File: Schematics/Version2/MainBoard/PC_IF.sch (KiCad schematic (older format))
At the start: 4 parts, among them U22 74F574, U23 74F574

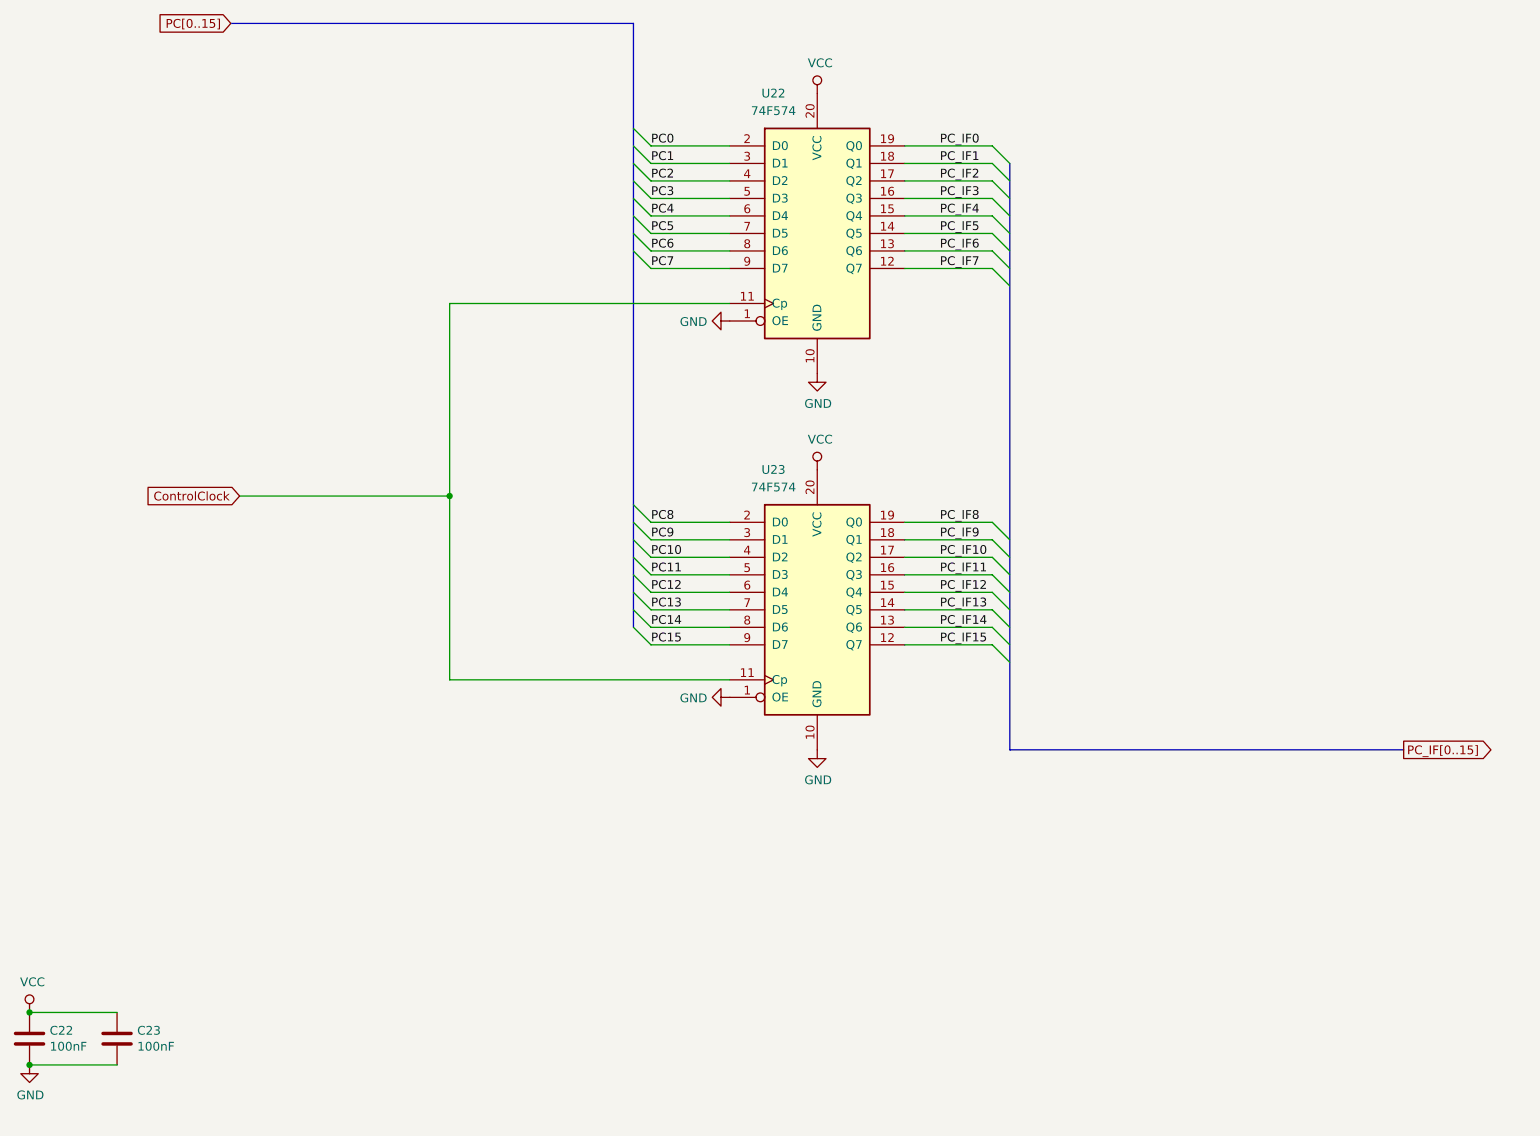
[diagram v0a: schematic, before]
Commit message: Merge branch "version2a"
This replaces the Version2 schematics with a new second version. This one
completes a four layer routing of the main board.
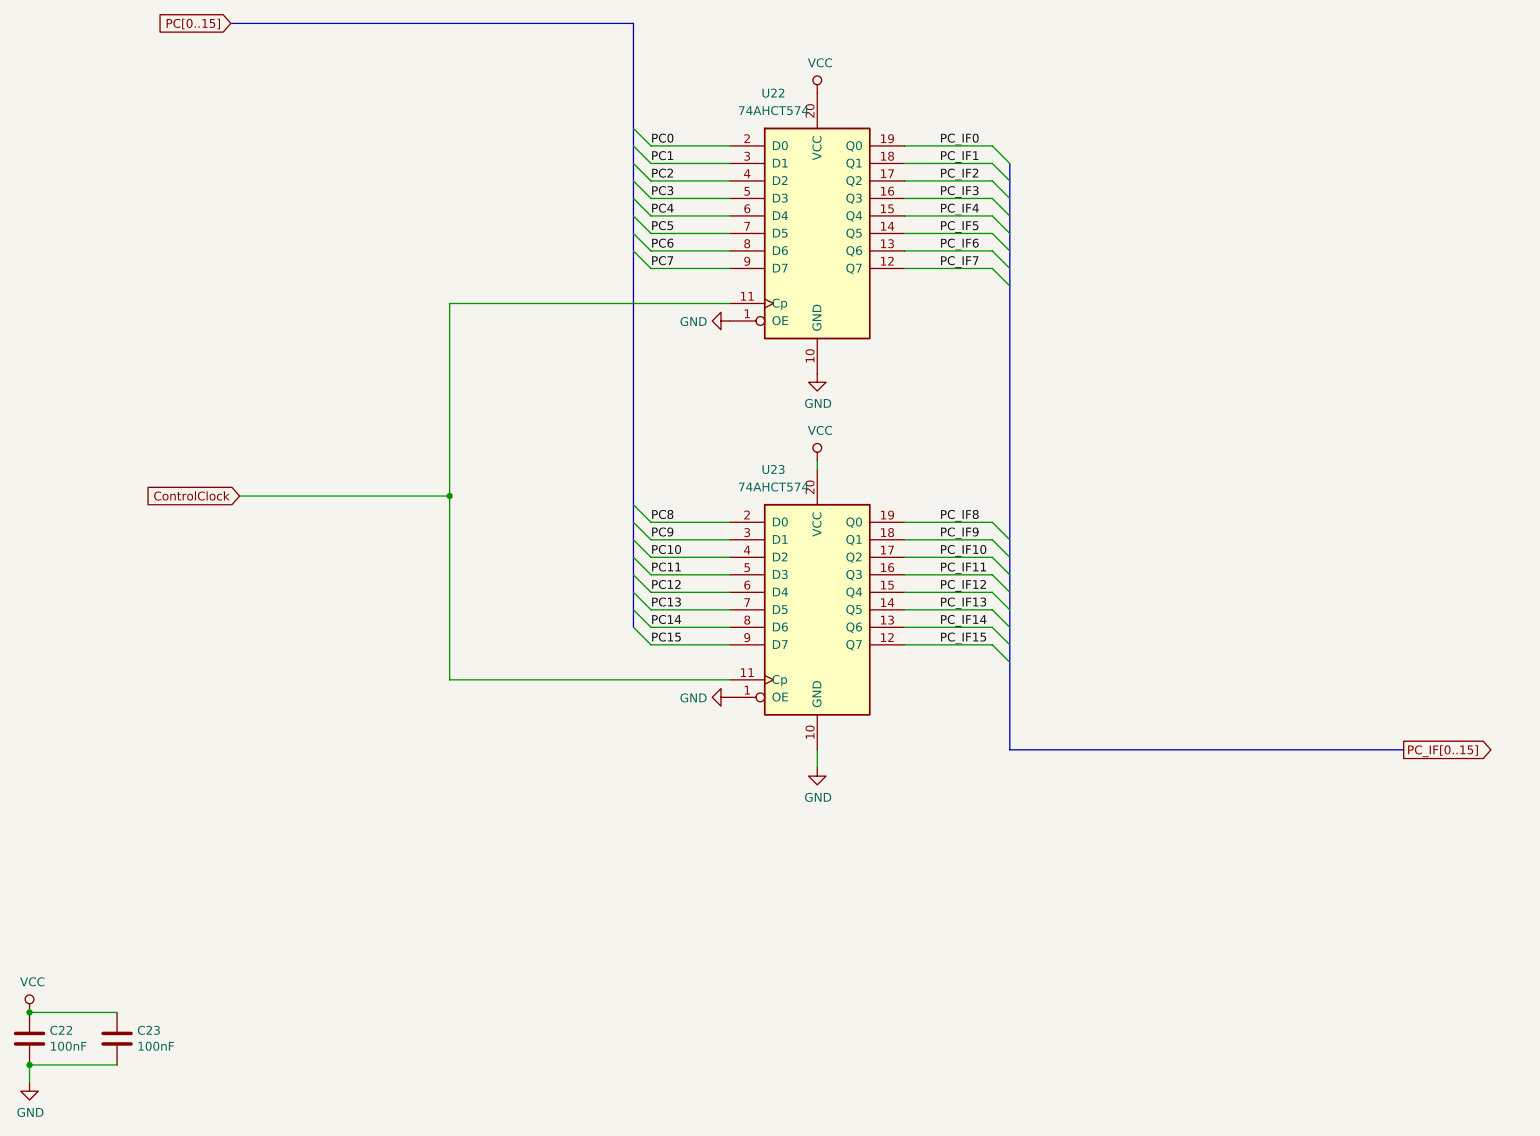
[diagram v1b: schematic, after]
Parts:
- U22, U23: value 74F574 -> 74AHCT574
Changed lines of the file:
@@
 $Descr USLetter 11000 8500
 encoding utf-8
-Sheet 6 22
+Sheet 6 23
 Title "PC/IF"
 Date ""
@@
 $EndComp
 $Comp
-L power:VCC #PWR058
-U 1 1 5DD11404
-P 5500 3900
-F 0 "#PWR058" H 5500 3750 50  0001 C CNN
-F 1 "VCC" H 5517 4073 50  0000 C CNN
-F 2 "" H 5500 3900 50  0001 C CNN
-F 3 "" H 5500 3900 50  0001 C CNN
-	1    5500 3900
-	1    0    0    -1
-$EndComp
-$Comp
 L power:GND #PWR057
 U 1 1 5DD11B50
@@
 L power:GND #PWR059
 U 1 1 5DD12126
-P 5500 5500
-F 0 "#PWR059" H 5500 5250 50  0001 C CNN
-F 1 "GND" H 5505 5327 50  0000 C CNN
-F 2 "" H 5500 5500 50  0001 C CNN
-F 3 "" H 5500 5500 50  0001 C CNN
-	1    5500 5500
+P 5500 5600
+F 0 "#PWR059" H 5500 5350 50  0001 C CNN
+F 1 "GND" H 5505 5427 50  0000 C CNN
+F 2 "" H 5500 5600 50  0001 C CNN
+F 3 "" H 5500 5600 50  0001 C CNN
+	1    5500 5600
 	1    0    0    -1
 $EndComp
@@
 $EndComp
 $Comp
-L power:GND #PWR053
-U 1 1 5DD314A1
-P 1000 7300
-F 0 "#PWR053" H 1000 7050 50  0001 C CNN
-F 1 "GND" H 1005 7127 50  0000 C CNN
-F 2 "" H 1000 7300 50  0001 C CNN
-F 3 "" H 1000 7300 50  0001 C CNN
-	1    1000 7300
-	1    0    0    -1
-$EndComp
-$Comp
 L power:VCC #PWR052
 U 1 1 5DD314A7
@@
 Wire Wire Line
 	1500 7300 1000 7300
-Connection ~ 1000 7300
 $Comp
 L 74xx:74LS574 U?
@@
 AR Path="/5D8005AF/5D833E4B/5D89A6E8" Ref="U22"  Part="1"
 F 0 "U22" H 5250 3350 50  0000 C CNN
-F 1 "74F574" H 5250 3250 50  0000 C CNN
+F 1 "74AHCT574" H 5250 3250 50  0000 C CNN
 F 2 "Package_DIP:DIP-20_W7.62mm" H 5500 2550 50  0001 C CNN
-F 3 "http://www.ti.com/lit/gpn/sn74LS574" H 5500 2550 50  0001 C CNN
+F 3 "http://www.ti.com/lit/ds/symlink/sn74ahct574.pdf" H 5500 2550 50  0001 C CNN
 	1    5500 2550
 	1    0    0    -1
@@
 AR Path="/5D8005AF/5D833E4B/5D89C1BF" Ref="U23"  Part="1"
 F 0 "U23" H 5250 5500 50  0000 C CNN
-F 1 "74F574" H 5250 5400 50  0000 C CNN
+F 1 "74AHCT574" H 5250 5400 50  0000 C CNN
 F 2 "Package_DIP:DIP-20_W7.62mm" H 5500 4700 50  0001 C CNN
-F 3 "http://www.ti.com/lit/gpn/sn74LS574" H 5500 4700 50  0001 C CNN
+F 3 "http://www.ti.com/lit/ds/symlink/sn74ahct574.pdf" H 5500 4700 50  0001 C CNN
 	1    5500 4700
 	1    0    0    -1
 $EndComp
+Wire Wire Line
+	5500 5500 5500 5600
+$Comp
+L power:VCC #PWR0241
+U 1 1 5E1D964A
+P 5500 3850
+F 0 "#PWR0241" H 5500 3700 50  0001 C CNN
+F 1 "VCC" H 5517 4023 50  0000 C CNN
+F 2 "" H 5500 3850 50  0001 C CNN
+F 3 "" H 5500 3850 50  0001 C CNN
+	1    5500 3850
+	1    0    0    -1
+$EndComp
+Wire Wire Line
+	5500 3850 5500 3900
+$Comp
+L power:GND #PWR0244
+U 1 1 5E1E7523
+P 1000 7400
+F 0 "#PWR0244" H 1000 7150 50  0001 C CNN
+F 1 "GND" H 1005 7227 50  0000 C CNN
+F 2 "" H 1000 7400 50  0001 C CNN
+F 3 "" H 1000 7400 50  0001 C CNN
+	1    1000 7400
+	1    0    0    -1
+$EndComp
+Wire Wire Line
+	1000 7400 1000 7300
+Connection ~ 1000 7300
 Wire Bus Line
 	4450 1350 4450 4800

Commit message: Merge branch "version2b".
This is a new version of the computer which incorporates a number of
improvements:
  * Uses a four layer PCB instead of six.
  * Replaced the clock with a new circuit. This is simpler, but allows for
    an external clock to be attached.
  * Changes to the ALU to have it operate over two clock cycles instead of
    one. This fixes a timing issue which makes the ALU unreliable at 10MHz.
  * Replaced instruction RAM with dual port SRAM.
  * Replaced the physical connector for expansion cards to interleave
    signals with ground.
  * Added places where components can be attached to provide AC termination
    of the data bus, should this be necessary.
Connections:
- net ControlClock renamed ControlClock3
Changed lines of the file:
@@
 $Descr USLetter 11000 8500
 encoding utf-8
-Sheet 6 23
+Sheet 5 21
 Title "PC/IF"
 Date ""
@@
 $EndComp
 Text GLabel 2200 4050 0    50   Input ~ 0
-ControlClock
+ControlClock3
 Wire Wire Line
 	5000 5100 3400 5100
